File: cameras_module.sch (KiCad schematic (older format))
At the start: 19 parts, among them J3 WE_68715014522, U4 PCA9547BS

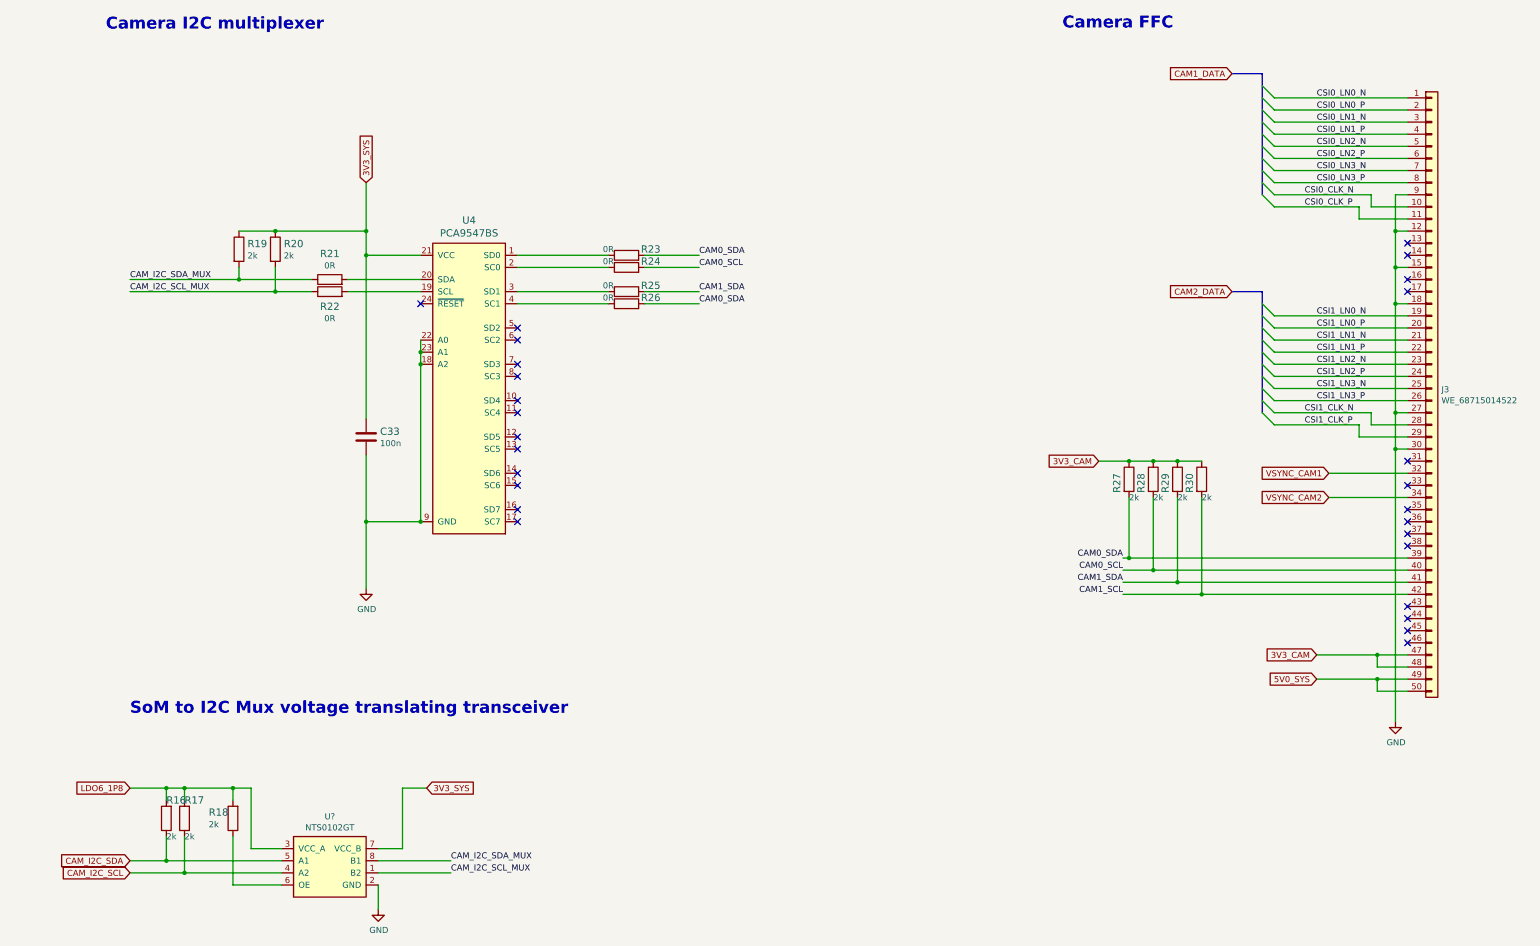
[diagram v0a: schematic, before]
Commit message: Added corrections to schemas after review
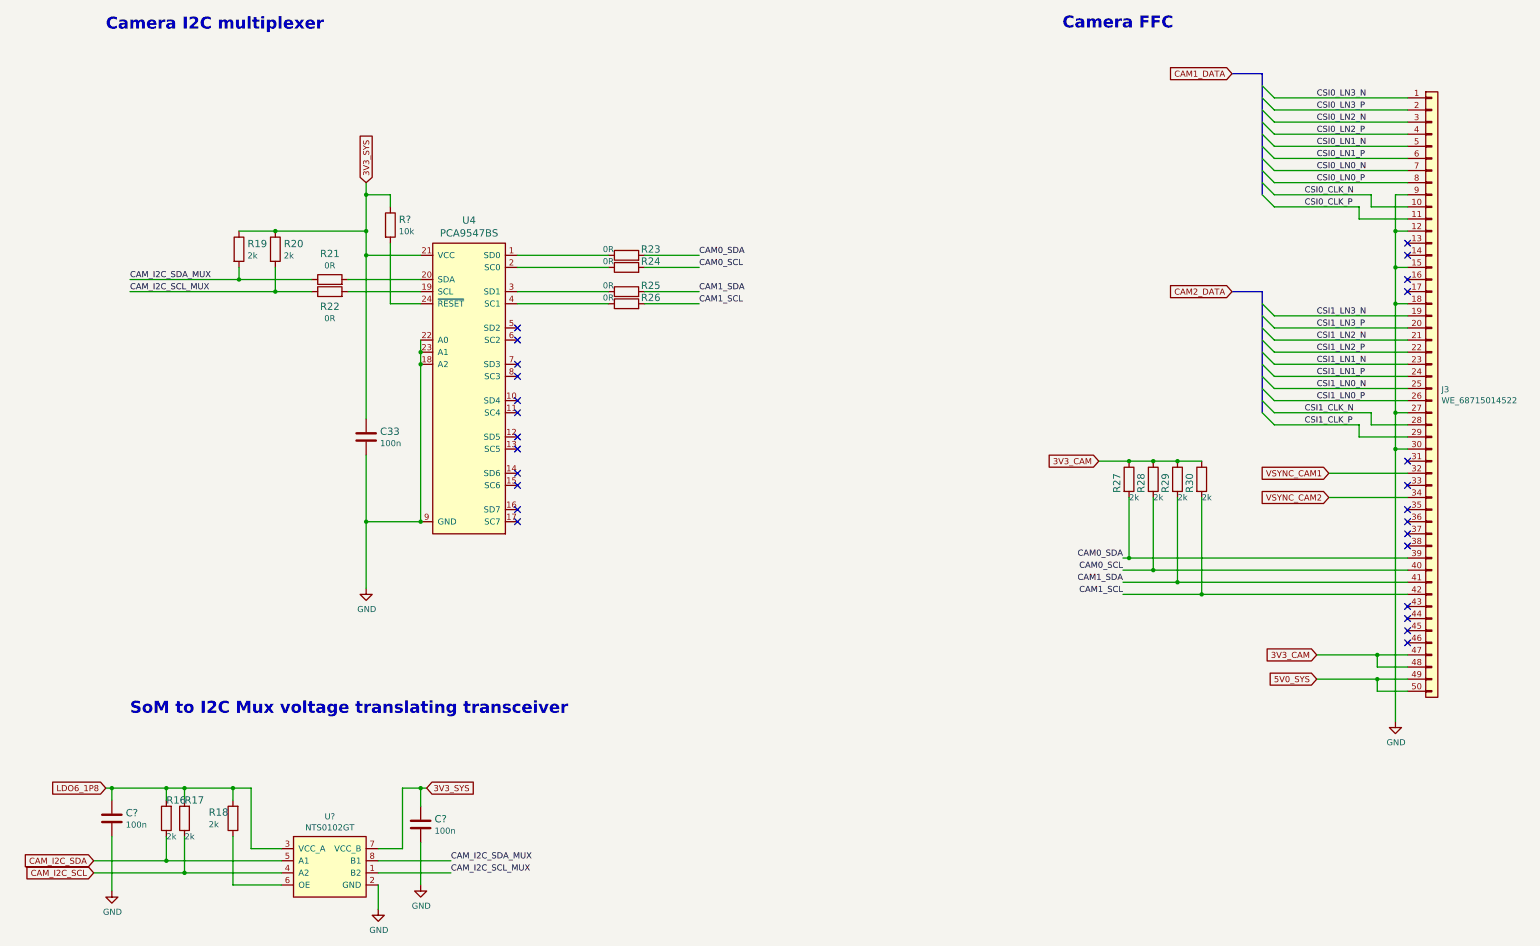
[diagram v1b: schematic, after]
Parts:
- added C? (x2): C_100n_0402, antmicro-footprints:0402-cap, symbol antmicroCapacitors0402:C_100n_0402
- added R?: R_10k_0402, antmicro-footprints:0402-res, symbol antmicroResistors0402:R_10k_0402
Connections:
- net 3V3_SYS: now also C?.1, R?.1
- net CAM0_SDA: no longer R26.2
- net CAM1_SCL: now also R26.2
- net CSI0_LN0_N: now also J3.7 (Pin_7); no longer J3.1 (Pin_1)
- net CSI0_LN0_P: now also J3.8 (Pin_8); no longer J3.2 (Pin_2)
- net CSI0_LN1_N: now also J3.5 (Pin_5); no longer J3.3 (Pin_3)
- net CSI0_LN1_P: now also J3.6 (Pin_6); no longer J3.4 (Pin_4)
- net CSI0_LN2_N: now also J3.3 (Pin_3); no longer J3.5 (Pin_5)
- net CSI0_LN2_P: now also J3.4 (Pin_4); no longer J3.6 (Pin_6)
- net CSI0_LN3_N: now also J3.1 (Pin_1); no longer J3.7 (Pin_7)
- net CSI0_LN3_P: now also J3.2 (Pin_2); no longer J3.8 (Pin_8)
- net CSI1_LN0_N: now also J3.25 (Pin_25); no longer J3.19 (Pin_19)
- net CSI1_LN0_P: now also J3.26 (Pin_26); no longer J3.20 (Pin_20)
- net CSI1_LN1_N: now also J3.23 (Pin_23); no longer J3.21 (Pin_21)
- net CSI1_LN1_P: now also J3.24 (Pin_24); no longer J3.22 (Pin_22)
- net CSI1_LN2_N: now also J3.21 (Pin_21); no longer J3.23 (Pin_23)
- net CSI1_LN2_P: now also J3.22 (Pin_22); no longer J3.24 (Pin_24)
- net CSI1_LN3_N: now also J3.19 (Pin_19); no longer J3.25 (Pin_25)
- net CSI1_LN3_P: now also J3.20 (Pin_20); no longer J3.26 (Pin_26)
- net GND: now also C?.2, C?.2
- net LDO6_1P8: now also C?.1
- net at U4.24 (~RESET): now also R?.2
- no-connect marks 27 -> 26
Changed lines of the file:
@@
 3V3_SYS
 Wire Wire Line
-	4000 3000 4000 3400
+	4000 3000 4000 3100
 Wire Wire Line
 	4450 3600 4000 3600
@@
 Wire Wire Line
 	4000 5800 4000 5250
-NoConn ~ 4450 4000
 NoConn ~ 5250 4200
 NoConn ~ 5250 4300
@@
 CAM1_SDA
 Text Label 6750 4000 0    50   ~ 0
-CAM0_SDA
+CAM1_SCL
 Wire Wire Line
 	6300 3600 6750 3600
@@
 	4100 8800 4100 9000
 Wire Wire Line
-	2050 8600 2350 8600
+	1750 8600 2350 8600
 Wire Wire Line
 	3300 8700 2500 8700
@@
 3V3_SYS
 Wire Wire Line
-	4500 8000 4300 8000
+	4500 8000 4450 8000
 Wire Wire Line
 	4300 8000 4300 8500
 Wire Wire Line
 	4300 8500 4100 8500
-Text GLabel 2050 8000 0    50   Input ~ 0
+Text GLabel 1850 8000 0    50   Input ~ 0
 LDO6_1P8
 Wire Wire Line
-	2050 8000 2350 8000
+	1850 8000 1900 8000
 Wire Wire Line
 	3050 8000 3050 8500
@@
 Connection ~ 2500 8700
 Wire Wire Line
-	2500 8700 2050 8700
-Text GLabel 2050 8600 0    50   Input ~ 0
+	2500 8700 1750 8700
+Text GLabel 1750 8600 0    50   Input ~ 0
 CAM_I2C_SDA
-Text GLabel 2050 8700 0    50   Input ~ 0
+Text GLabel 1750 8700 0    50   Input ~ 0
 CAM_I2C_SCL
 $Comp
@@
 	11400 3100 11500 3200
 Wire Wire Line
+	11500 2900 12600 2900
+Wire Wire Line
+	12600 3000 11500 3000
+Wire Wire Line
+	11500 2700 12600 2700
+Wire Wire Line
+	12600 2800 11500 2800
+Wire Wire Line
+	11500 2500 12600 2500
+Wire Wire Line
+	12600 2600 11500 2600
+Wire Wire Line
 	11500 2300 12600 2300
 Wire Wire Line
 	12600 2400 11500 2400
 Wire Wire Line
-	11500 2500 12600 2500
-Wire Wire Line
-	12600 2600 11500 2600
-Wire Wire Line
-	11500 2700 12600 2700
-Wire Wire Line
-	12600 2800 11500 2800
-Wire Wire Line
-	11500 2900 12600 2900
-Wire Wire Line
-	12600 3000 11500 3000
-Wire Wire Line
 	12600 3200 12300 3200
 Wire Wire Line
@@
 Wire Wire Line
 	12200 3200 11500 3200
+Text Label 11850 2900 0    50   ~ 0
+CSI0_LN0_N
+Text Label 11850 3000 0    50   ~ 0
+CSI0_LN0_P
+Text Label 11850 2700 0    50   ~ 0
+CSI0_LN1_N
+Text Label 11850 2800 0    50   ~ 0
+CSI0_LN1_P
+Text Label 11850 2500 0    50   ~ 0
+CSI0_LN2_N
+Text Label 11850 2600 0    50   ~ 0
+CSI0_LN2_P
 Text Label 11850 2300 0    50   ~ 0
-CSI0_LN0_N
+CSI0_LN3_N
 Text Label 11850 2400 0    50   ~ 0
-CSI0_LN0_P
-Text Label 11850 2500 0    50   ~ 0
-CSI0_LN1_N
-Text Label 11850 2600 0    50   ~ 0
-CSI0_LN1_P
-Text Label 11850 2700 0    50   ~ 0
-CSI0_LN2_N
-Text Label 11850 2800 0    50   ~ 0
-CSI0_LN2_P
-Text Label 11850 2900 0    50   ~ 0
-CSI0_LN3_N
-Text Label 11850 3000 0    50   ~ 0
 CSI0_LN3_P
 Text Label 11750 3100 0    50   ~ 0
@@
 	11400 4900 11500 5000
 Wire Wire Line
+	11500 4700 12600 4700
+Wire Wire Line
+	12600 4800 11500 4800
+Wire Wire Line
+	11500 4500 12600 4500
+Wire Wire Line
+	12600 4600 11500 4600
+Wire Wire Line
+	11500 4300 12600 4300
+Wire Wire Line
+	12600 4400 11500 4400
+Wire Wire Line
 	11500 4100 12600 4100
 Wire Wire Line
 	12600 4200 11500 4200
 Wire Wire Line
-	11500 4300 12600 4300
-Wire Wire Line
-	12600 4400 11500 4400
-Wire Wire Line
-	11500 4500 12600 4500
-Wire Wire Line
-	12600 4600 11500 4600
-Wire Wire Line
-	11500 4700 12600 4700
-Wire Wire Line
-	12600 4800 11500 4800
-Wire Wire Line
 	12600 5000 12300 5000
 Wire Wire Line
@@
 Wire Wire Line
 	12200 5000 11500 5000
+Text Label 11850 4700 0    50   ~ 0
+CSI1_LN0_N
+Text Label 11850 4800 0    50   ~ 0
+CSI1_LN0_P
+Text Label 11850 4500 0    50   ~ 0
+CSI1_LN1_N
+Text Label 11850 4600 0    50   ~ 0
+CSI1_LN1_P
+Text Label 11850 4300 0    50   ~ 0
+CSI1_LN2_N
+Text Label 11850 4400 0    50   ~ 0
+CSI1_LN2_P
 Text Label 11850 4100 0    50   ~ 0
-CSI1_LN0_N
+CSI1_LN3_N
 Text Label 11850 4200 0    50   ~ 0
-CSI1_LN0_P
-Text Label 11850 4300 0    50   ~ 0
-CSI1_LN1_N
-Text Label 11850 4400 0    50   ~ 0
-CSI1_LN1_P
-Text Label 11850 4500 0    50   ~ 0
-CSI1_LN2_N
-Text Label 11850 4600 0    50   ~ 0
-CSI1_LN2_P
-Text Label 11850 4700 0    50   ~ 0
-CSI1_LN3_N
-Text Label 11850 4800 0    50   ~ 0
 CSI1_LN3_P
 Text Label 11750 4900 0    50   ~ 0
@@
 	1    0    0    -1
 $EndComp
+$Comp
+L antmicroResistors0402:R_10k_0402 R?
+U 1 1 62145419
+P 4200 3350
+F 0 "R?" V 4155 3420 60  0000 L CNN
+F 1 "R_10k_0402" H 4200 3200 60  0001 C CNN
+F 2 "antmicro-footprints:0402-res" H 4400 3550 60  0001 L CNN
+F 3 "" H 4200 3350 50  0001 C CNN
+F 4 "VISHAY" H 4400 3750 60  0001 L CNN "Manufacturer"
+F 5 "CRCW040210K0FKEDHP" H 4400 3650 60  0001 L CNN "MPN"
+F 6 "10k" V 4253 3420 50  0000 L CNN "Val"
+	1    4200 3350
+	0    1    1    0
+$EndComp
+Wire Wire Line
+	4200 3500 4200 4000
+Wire Wire Line
+	4200 4000 4450 4000
+Wire Wire Line
+	4200 3200 4200 3100
+Wire Wire Line
+	4200 3100 4000 3100
+Connection ~ 4000 3100
+Wire Wire Line
+	4000 3100 4000 3400
+$Comp
+L antmicroCapacitors0402:C_100n_0402 C?
+U 1 1 6214EFB5
+P 4450 8300
+F 0 "C?" H 4565 8345 60  0000 L CNN
+F 1 "C_100n_0402" H 4450 8150 60  0001 C CNN
+F 2 "antmicro-footprints:0402-cap" H 4650 8500 60  0001 L CNN
+F 3 "" H 4450 8300 50  0001 C CNN
+F 4 "Murata" H 4650 8700 60  0001 L CNN "Manufacturer"
+F 5 "GRM155R61H104KE14D" H 4650 8600 60  0001 L CNN "MPN"
+F 6 "100n" H 4565 8247 50  0000 L CNN "Val"
+	1    4450 8300
+	1    0    0    -1
+$EndComp
+$Comp
+L antmicroCapacitors0402:C_100n_0402 C?
+U 1 1 6214F58A
+P 1900 8250
+F 0 "C?" H 2015 8295 60  0000 L CNN
+F 1 "C_100n_0402" H 1900 8100 60  0001 C CNN
+F 2 "antmicro-footprints:0402-cap" H 2100 8450 60  0001 L CNN
+F 3 "" H 1900 8250 50  0001 C CNN
+F 4 "Murata" H 2100 8650 60  0001 L CNN "Manufacturer"
+F 5 "GRM155R61H104KE14D" H 2100 8550 60  0001 L CNN "MPN"
+F 6 "100n" H 2015 8197 50  0000 L CNN "Val"
+	1    1900 8250
+	1    0    0    -1
+$EndComp
+$Comp
+L sc606-baseboard:GND #PWR?
+U 1 1 6215CCFC
+P 4450 8800
+F 0 "#PWR?" H 4450 8550 50  0001 C CNN
+F 1 "GND" H 4455 8627 50  0000 C CNN
+F 2 "" H 4450 8800 50  0001 C CNN
+F 3 "" H 4450 8800 50  0001 C CNN
+	1    4450 8800
+	1    0    0    -1
+$EndComp
+$Comp
+L sc606-baseboard:GND #PWR?
+U 1 1 62161810
+P 1900 8850
+F 0 "#PWR?" H 1900 8600 50  0001 C CNN
+F 1 "GND" H 1905 8677 50  0000 C CNN
+F 2 "" H 1900 8850 50  0001 C CNN
+F 3 "" H 1900 8850 50  0001 C CNN
+	1    1900 8850
+	1    0    0    -1
+$EndComp
+Wire Wire Line
+	1900 8850 1900 8400
+Wire Wire Line
+	1900 8100 1900 8000
+Connection ~ 1900 8000
+Wire Wire Line
+	1900 8000 2350 8000
+Wire Wire Line
+	4450 8150 4450 8000
+Connection ~ 4450 8000
+Wire Wire Line
+	4450 8000 4300 8000
+Wire Wire Line
+	4450 8450 4450 8800
 Wire Bus Line
 	11400 2100 11400 3100

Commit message: Chip changed for Debug UART. Changed connector from USB-A to USB-C
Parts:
- C? (x2): footprint antmicro-footprints:0402-cap -> sc606-baseboard-footprints:0402-cap; symbol antmicroCapacitors0402:C_100n_0402 -> sc606-baseboard:C_100n_0402
- R?: footprint antmicro-footprints:0402-res -> sc606-baseboard-footprints:0402-res; symbol antmicroResistors0402:R_10k_0402 -> sc606-baseboard:R_10k_0402
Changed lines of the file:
@@
 $EndComp
 $Comp
-L antmicroResistors0402:R_10k_0402 R?
+L sc606-baseboard:R_10k_0402 R?
 U 1 1 62145419
 P 4200 3350
 F 0 "R?" V 4155 3420 60  0000 L CNN
 F 1 "R_10k_0402" H 4200 3200 60  0001 C CNN
-F 2 "antmicro-footprints:0402-res" H 4400 3550 60  0001 L CNN
+F 2 "sc606-baseboard-footprints:0402-res" H 4400 3550 60  0001 L CNN
 F 3 "" H 4200 3350 50  0001 C CNN
 F 4 "VISHAY" H 4400 3750 60  0001 L CNN "Manufacturer"
@@
 	4000 3100 4000 3400
 $Comp
-L antmicroCapacitors0402:C_100n_0402 C?
+L sc606-baseboard:C_100n_0402 C?
 U 1 1 6214EFB5
 P 4450 8300
 F 0 "C?" H 4565 8345 60  0000 L CNN
 F 1 "C_100n_0402" H 4450 8150 60  0001 C CNN
-F 2 "antmicro-footprints:0402-cap" H 4650 8500 60  0001 L CNN
+F 2 "sc606-baseboard-footprints:0402-cap" H 4650 8500 60  0001 L CNN
 F 3 "" H 4450 8300 50  0001 C CNN
 F 4 "Murata" H 4650 8700 60  0001 L CNN "Manufacturer"
@@
 $EndComp
 $Comp
-L antmicroCapacitors0402:C_100n_0402 C?
+L sc606-baseboard:C_100n_0402 C?
 U 1 1 6214F58A
 P 1900 8250
 F 0 "C?" H 2015 8295 60  0000 L CNN
 F 1 "C_100n_0402" H 1900 8100 60  0001 C CNN
-F 2 "antmicro-footprints:0402-cap" H 2100 8450 60  0001 L CNN
+F 2 "sc606-baseboard-footprints:0402-cap" H 2100 8450 60  0001 L CNN
 F 3 "" H 1900 8250 50  0001 C CNN
 F 4 "Murata" H 2100 8650 60  0001 L CNN "Manufacturer"
